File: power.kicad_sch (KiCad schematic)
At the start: 27 parts, among them J14 DeployLipo, J15 UCLipo, Q10 AO3401A, Q7 SI4143DY-T1-GE3, Q8 SI4143DY-T1-GE3, Q9 AO3401A, U10 LTC4411ES5TRMPBF, U11 LTC4411ES5TRMPBF, U12 LT1963AxST-3.3, U13 LTC4412xS6, U14 LTC4412xS6, U15 LTC4412xS6, U16 LTC4412xS6

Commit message: working on v2
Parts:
- removed C19, C20: 1uF, Capacitor_SMD:C_0603_1608Metric, symbol Device:C_Small
- removed C21, C22: 4.7uF, Capacitor_SMD:C_0603_1608Metric, symbol Device:C_Small
- removed H1, H2, H3, H4: MountingHole_Pad, MountingHole:MountingHole_3.2mm_M3_DIN965_Pad, symbol Mechanical:MountingHole_Pad
- removed J14: DeployLipo, TerminalBlock_Phoenix:TerminalBlock_Phoenix_MKDS-3-2-5.08_1x02_P5.08mm_Horizontal, symbol Connector:Conn_01x02_Male
- removed J15: UCLipo, Connector_JST:JST_PH_B2B-PH-K_1x02_P2.00mm_Vertical, symbol Connector:Conn_01x02_Male
- removed JP2: SolderJumper_2_Open, Jumper:SolderJumper-2_P1.3mm_Open_RoundedPad1.0x1.5mm, symbol Jumper:SolderJumper_2_Open
- removed Q10, Q9: AO3401A, Package_TO_SOT_SMD:SOT-23, symbol Transistor_FET:AO3401A
- removed Q7, Q8: SI4143DY-T1-GE3, Package_SO:SOIC-8_3.9x4.9mm_P1.27mm, symbol Device:Q_PMOS_GDS
- removed R23: 7.5k, Resistor_SMD:R_0603_1608Metric, symbol Device:R_Small
- removed R24: 2.4k, Resistor_SMD:R_0603_1608Metric, symbol Device:R_Small
- removed U10, U11: LTC4411ES5TRMPBF, Package_TO_SOT_SMD:SOT-23-5_HandSoldering, symbol LTC4411ES5TRMPBF:LTC4411ES5TRMPBF
- removed U12: LT1963AxST-3.3, Package_TO_SOT_SMD:SOT-223-3_TabPin2, symbol Regulator_Linear:LT1963AxST-3.3
- removed U13, U14, U15, U16: LTC4412xS6, Package_TO_SOT_SMD:TSOT-23-6, symbol Power_Management:LTC4412xS6
- added C23, C29: 4.7uF, Capacitor_SMD:C_0402_1005Metric, symbol Device:C_Small
- added C27: 22uF, Capacitor_SMD:C_0603_1608Metric, symbol Device:C_Small
- added C28, C30: 10uF, Capacitor_SMD:C_0402_1005Metric, symbol Device:C_Small
- added C31: 0.1uF, Capacitor_SMD:C_0402_1005Metric, symbol Device:C_Small
- added C? (x2): 1uF, Capacitor_SMD:C_0603_1608Metric, symbol Device:C_Small
- added C? (x2): 10uF, Capacitor_SMD:C_0603_1608Metric, symbol Device:C_Small
- added C? (x2): 4.7uF, Capacitor_SMD:C_0603_1608Metric, symbol Device:C_Small
- added C?: 100nF, Capacitor_SMD:C_0603_1608Metric, symbol Device:C_Small
- added H? (x4): MountingHole_Pad, MountingHole:MountingHole_3.2mm_M3_DIN965_Pad, symbol Mechanical:MountingHole_Pad
- added J?: UCLipo, Connector_JST:JST_PH_B2B-PH-K_1x02_P2.00mm_Vertical, symbol Connector:Conn_01x02_Male
- added J?: DeployLipo, TerminalBlock_Phoenix:TerminalBlock_Phoenix_MKDS-3-2-5.08_1x02_P5.08mm_Horizontal, symbol Connector:Conn_01x02_Male
- added JP?: SolderJumper_2_Open, Jumper:SolderJumper-2_P1.3mm_Open_RoundedPad1.0x1.5mm, symbol Jumper:SolderJumper_2_Open
- added L3: 1uH, Inductor_SMD:L_0805_2012Metric, symbol Device:L
- added Q? (x2): AO3401A, Package_TO_SOT_SMD:SOT-23, symbol Transistor_FET:AO3401A
- added Q? (x2): SI4143DY-T1-GE3, Package_SO:SOIC-8_3.9x4.9mm_P1.27mm, symbol Device:Q_PMOS_GDS
- added R16: 14k, Resistor_SMD:R_0402_1005Metric, symbol Device:R_Small
- added R17: 56k, Resistor_SMD:R_0402_1005Metric, symbol Device:R_Small
- added R18: 10k, Resistor_SMD:R_0402_1005Metric, symbol Device:R_Small
- added R?: 7.5k, Resistor_SMD:R_0603_1608Metric, symbol Device:R_Small
- added R?: 2.4k, Resistor_SMD:R_0603_1608Metric, symbol Device:R_Small
- added TP4, TP5, TP6, TP7, TP8: TestPoint, TestPoint:TestPoint_Pad_D1.5mm, symbol Connector:TestPoint
- added U5, U6: LM66100, Package_TO_SOT_SMD:SOT-23-5, symbol iclr:LTC4411
- added U7: MAX77827AEFD+T, iclr:CONV_MAX77827AEFD+T, symbol iclr:MAX77827AEFD+T
- added U8: SC4215, iclr:SOIC127P599X175-9N, symbol iclr:RT9025-25GSP
- added U? (x2): LTC4411ES5TRMPBF, Package_TO_SOT_SMD:SOT-23-5_HandSoldering, symbol LTC4411ES5TRMPBF:LTC4411ES5TRMPBF
- added U? (x4): LTC4412xS6, Package_TO_SOT_SMD:TSOT-23-6, symbol Power_Management:LTC4412xS6
- added U?: LT1963AxST-3.3, Package_TO_SOT_SMD:SOT-223-3_TabPin2, symbol Regulator_Linear:LT1963AxST-3.3
- C24: value 10uF -> 4.7uF; footprint Capacitor_SMD:C_0603_1608Metric -> Capacitor_SMD:C_0402_1005Metric
- C26: value 100nF -> 1uF; footprint Capacitor_SMD:C_0603_1608Metric -> Capacitor_SMD:C_0402_1005Metric
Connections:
- net +24V: now also Q?.5 (D), Q?.5 (D), Q?.6 (D), Q?.6 (D), Q?.7 (D), Q?.7 (D), Q?.8 (D), Q?.8 (D), U?.6 (SENSE), U?.6 (SENSE)
- net +3V3: now also C30.2, C31.2, C?.1, C?.1, R17.1, TP6.1, U8.6 (VOUT), U?.5 (OUT), U?.5 (OUT)
- net 3.3reg_in: now also C?.2, Q?.2 (S), Q?.2 (S), U?.1 (IN), U?.6 (SENSE), U?.6 (SENSE); no longer C24.2
- net 3.3reg_out: now also C?.1, C?.2, C?.2, U?.1 (IN), U?.3 (OUT); no longer C25.2, C26.2
- net Deploy_Lipo+: now also J?.1 (Pin_1), JP?.1 (A), Q?.1 (S), Q?.2 (S), Q?.3 (S), U?.1 (VIN)
- net GND: now also C24.2, C25.2, C26.2, C23.2, C27.2, C28.2, C29.2, C30.1, C31.1, C?.1, C?.1, C?.1, C?.2, C?.2, C?.2, C?.2, H?.1, H?.1, H?.1, H?.1, J?.2 (Pin_2), J?.2 (Pin_2), R16.2, R18.2, R?.2, U5.2 (GND), U5.3 (CTL), U6.2 (GND), U6.3 (CTL), U7.4 (AGND), U7.9 (PGND), U8.8 (GND), U8.9 (GND), U?.2 (GND), U?.2 (GND), U?.2 (GND), U?.2 (GND), U?.2 (GND), U?.2 (GND), U?.2 (GND), U?.3 (CTL), U?.3 (CTL), U?.3 (CTL), U?.3 (CTL), U?.3 (CTL), U?.3 (CTL); no longer C24.1, C25.1, C26.1
- net RBUS_24V_IN: now also Q?.1 (S), Q?.2 (S), Q?.3 (S), U?.1 (VIN)
- net RBUS_3.3_IN: now also C?.1, U?.1 (IN)
- net UC_Lipo+: now also J?.1 (Pin_1), JP?.2 (B), Q?.3 (D), R?.1, U?.1 (VIN)
- net UC_Lipo_Scaled: now also R?.1, R?.2
- net VBUS: now also Q?.3 (D), TP7.1, U6.1 (IN), U?.1 (VIN)
- new net: Q?.1 (G), U?.5 (GATE) (x2)
- new net: Q?.4 (G), U?.5 (GATE) (x2)
- new net BBIN: C23.1, C24.1, C25.1, TP4.1, U5.5 (OUT), U6.5 (OUT), U7.3 (EN), U7.6 (IN)
- new net BBOUT: C27.1, C28.1, C29.1, TP8.1, U7.11 (OUT), U7.13 (OUTS), U8.2 (EN), U8.3 (VIN)
- new net BIAS: C26.1, U7.5 (BIAS)
- new net FBIn: R17.2, R18.1, U8.7 (ADJ)
- new net LX1: L3.1, U7.8 (LX1)
- new net LX2: L3.2, U7.10 (LX2)
- new net RBUS_uC_V: TP5.1, U5.1 (IN)
- new net SEL: R16.1, U7.1 (SEL)
- no-connect marks 5 -> 11
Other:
- note added: "Be extra careful in leaving this connected at a single point"

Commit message: v2 time
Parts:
- removed C24: 4.7uF, Capacitor_SMD:C_0402_1005Metric, symbol Device:C_Small
- removed C? (x2): 1uF, Capacitor_SMD:C_0603_1608Metric, symbol Device:C_Small
- removed C? (x2): 4.7uF, Capacitor_SMD:C_0603_1608Metric, symbol Device:C_Small
- removed Q? (x2): AO3401A, Package_TO_SOT_SMD:SOT-23, symbol Transistor_FET:AO3401A
- removed U5, U6: LM66100, Package_TO_SOT_SMD:SOT-23-5, symbol iclr:LTC4411
- removed U? (x2): LTC4411ES5TRMPBF, Package_TO_SOT_SMD:SOT-23-5_HandSoldering, symbol LTC4411ES5TRMPBF:LTC4411ES5TRMPBF
- removed U? (x2): LTC4412xS6, Package_TO_SOT_SMD:TSOT-23-6, symbol Power_Management:LTC4412xS6
- removed U?: LT1963AxST-3.3, Package_TO_SOT_SMD:SOT-223-3_TabPin2, symbol Regulator_Linear:LT1963AxST-3.3
- added C29, C30, C31, C35, C36, C38, C41, C47, C48: 0.1uF, Capacitor_SMD:C_0402_1005Metric, symbol Device:C_Small
- added JP1: SolderJumper_3_Bridged12, Jumper:SolderJumper-3_P1.3mm_Bridged12_RoundedPad1.0x1.5mm, symbol Jumper:SolderJumper_3_Bridged12
- added U10: NCP1117-3.3_SOT223, Package_TO_SOT_SMD:SOT-223-3_TabPin2, symbol Regulator_Linear:NCP1117-3.3_SOT223
- added U11, U12, U13, U18, U9: XC8111, Package_TO_SOT_SMD:SOT-23-5, symbol Analog_Switch:MAX40200AUK
- C32, C33, C37: renamed from C?; footprint Capacitor_SMD:C_0603_1608Metric -> Capacitor_SMD:C_0402_1005Metric
- C34: renamed from C23; value 4.7uF -> 0.1uF
- R25: renamed from R?; value 7.5k -> 51k; footprint Resistor_SMD:R_0603_1608Metric -> Resistor_SMD:R_0402_1005Metric
- R26: renamed from R?; value 2.4k -> 10k; footprint Resistor_SMD:R_0603_1608Metric -> Resistor_SMD:R_0402_1005Metric
- gave numbers to parts that had none: 11
- renumbered C25 to C39, C26 to C40, C27 to C42, C28 to C43, C29 to C44, C30 to C45, C31 to C46, R16 to R27, R17 to R28, R18 to R29, TP4 to TP10, TP5 to TP11, TP7 to TP12, TP8 to TP13, TP6 to TP14, U7 to U15, U8 to U16
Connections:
- net +3V3: now also C41.1, C48.1, U13.5 (OUT), U18.5 (OUT); no longer C45.2, C46.2, R28.1, U16.6 (VOUT)
- net BBIN: now also C35.1, C36.1, U11.5 (OUT), U12.5 (OUT), U9.5 (OUT)
- net GND: now also C29.2, C30.2, C31.2, C35.2, C36.2, C38.1, C41.2, C47.1, C48.2, U10.1 (GND), U11.2 (GND), U12.2 (GND), U13.2 (GND), U18.2 (GND)
- net UC_Lipo+: now also JP1.2 (C)
- net VBUS: now also C31.1, U9.1 (VDD), U9.3 (EN)
- net 3.3reg_in: no longer names the net of C32.2
- net 3.3reg_in: now also JP1.3 (B), U10.3 (VI)
- net 3.3reg_out: no longer names the net of C33.2, C37.2
- net 3.3reg_out: now also C38.2, U10.2 (VO), U13.1 (VDD), U13.3 (EN)
- net RBUS_uC_V renamed RBUS_3.3V_IN
- net RBUS_3.3V_IN: now also C30.1, U11.1 (VDD), U11.3 (EN)
- new net: C45.2, C46.2, C47.2, R28.1, U16.6 (VOUT), U18.1 (VDD), U18.3 (EN)
- new net: C29.1, JP1.1 (A), U12.1 (VDD), U12.3 (EN)
- no-connect marks 11 -> 5
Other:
- note added: "Allows a voltage range of up to 20v -> 20v is scaled to 3.279v"
- note removed: "Allows a voltage range of up to 13v -> 13v is scaled to 3.3v"
- moved on the sheet: C32, C33, C34, C37, C39, C40, C42, C43, C44, C45, C46, H1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

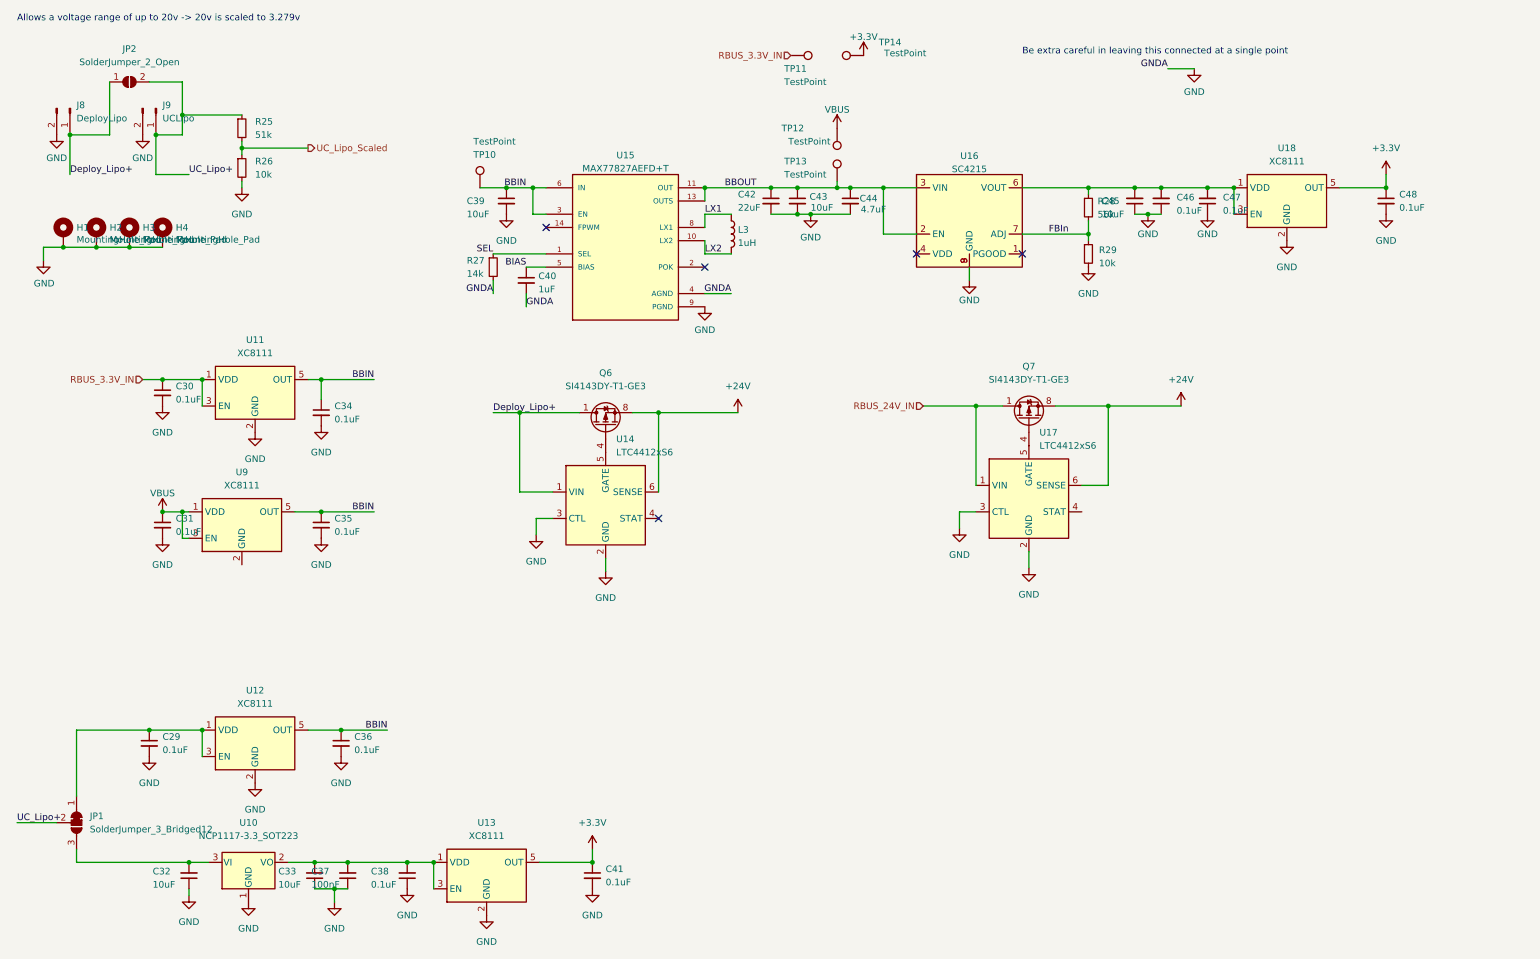
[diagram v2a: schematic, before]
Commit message: Conitnued with v2, NB pinout of external sd card has changed!!! Chest needs to be updated before manufacturing!!!
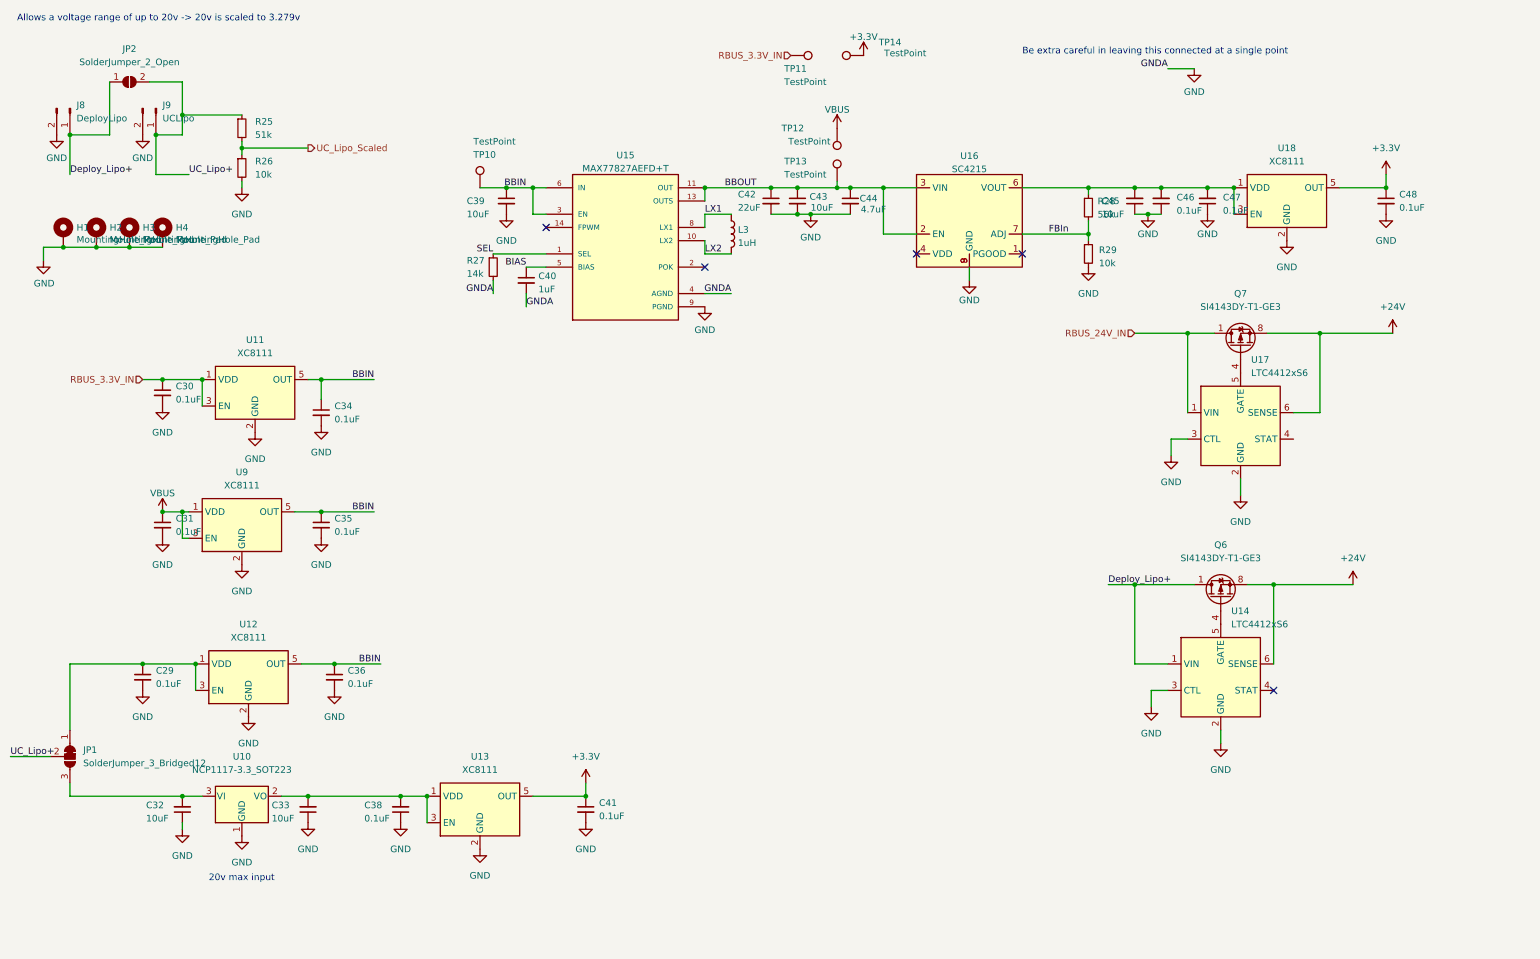
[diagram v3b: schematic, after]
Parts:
- removed C37: 100nF, Capacitor_SMD:C_0402_1005Metric, symbol Device:C_Small
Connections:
- net GND: now also U9.2 (GND)
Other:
- note added: "20v max input"
- moved on the sheet: C29, C32, C33, C36, C38, C41, JP1, Q6, Q7, U10, U12, U13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

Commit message: all components basically routed and fitted onto pickle v2
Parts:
- TP10, TP11, TP12, TP13, TP14: footprint TestPoint:TestPoint_Pad_D1.5mm -> TestPoint:TestPoint_Pad_D1.0mm
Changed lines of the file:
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@@
       (effects (font (size 1.27 1.27)) (justify left))
     )
-    (property "Footprint" "TestPoint:TestPoint_Pad_D1.5mm" (id 2) (at 177.8 49.53 0)
+    (property "Footprint" "TestPoint:TestPoint_Pad_D1.0mm" (id 2) (at 177.8 49.53 0)
       (effects (font (size 1.27 1.27)) hide)
     )
@@
       (effects (font (size 1.27 1.27)) (justify left))
     )
-    (property "Footprint" "TestPoint:TestPoint_Pad_D1.5mm" (id 2) (at 163.83 30.48 0)
+    (property "Footprint" "TestPoint:TestPoint_Pad_D1.0mm" (id 2) (at 163.83 30.48 0)
       (effects (font (size 1.27 1.27)) hide)
     )
@@
       (effects (font (size 1.27 1.27)) (justify left))
     )
-    (property "Footprint" "TestPoint:TestPoint_Pad_D1.5mm" (id 2) (at 109.22 50.8 0)
+    (property "Footprint" "TestPoint:TestPoint_Pad_D1.0mm" (id 2) (at 109.22 50.8 0)
       (effects (font (size 1.27 1.27)) hide)
     )
@@
       (effects (font (size 1.27 1.27)) (justify left))
     )
-    (property "Footprint" "TestPoint:TestPoint_Pad_D1.5mm" (id 2) (at 167.64 39.37 0)
+    (property "Footprint" "TestPoint:TestPoint_Pad_D1.0mm" (id 2) (at 167.64 39.37 0)
       (effects (font (size 1.27 1.27)) hide)
     )
@@
     (property "Reference" "TP14" (id 0) (at 182.88 22.86 90))
     (property "Value" "TestPoint" (id 1) (at 185.801 24.9616 90))
-    (property "Footprint" "TestPoint:TestPoint_Pad_D1.5mm" (id 2) (at 177.8 20.32 0)
-      (effects (font (size 1.27 1.27)) hide)
-    )
+    (property "Footprint" "TestPoint:TestPoint_Pad_D1.0mm" (id 2) (at 177.8 20.32 0)
+      (effects (font (size 1.27 1.27)) hide)
+    )
